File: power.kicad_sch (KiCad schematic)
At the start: 0 parts

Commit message: [#99756] Implement Power section schematic
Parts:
- added C601, C602, C603, C608, C609, C610, C612, C613, C614, C616, C619, C620, C625, C627, C629, C631, C633, C634, C635, C636: C_22u_16V_0603, antmicro-footprints:C_0603_1608Metric_EIA, symbol antmicroCapacitors0603:C_22u_16V_0603
- added C604, C605, C606, C607, C611, C615, C618, C621, C626, C628, C630, C632: C_100n_0402, antmicro-footprints:C_0402_1005Metric, symbol antmicroCapacitors0402:C_100n_0402
- added C617, C622, C623, C624: C_1u_25V_0402, antmicro-footprints:C_0402_1005Metric, symbol antmicroCapacitors0402:C_1u_25V_0402
- added L605: L_2u2_6.3A_Bourns-SRN8040, antmicro-footprints:L_Bourns-SRN8040, symbol antmicroFixedInductors:L_2u2_6.3A_Bourns-SRN8040
- added L606, L607, L608: L_2u2_1.5A_0806, antmicro-footprints:L_0806_2016Metric, symbol antmicroFixedInductors:L_2u2_1.5A_0806
- added R601, R602, R603, R604: R_0R_22.4A_0603, antmicro-footprints:R_0603_1608Metric, symbol antmicroResistors0603:R_0R_22.4A_0603
- added R605: R_255k_0402, antmicro-footprints:R_0402_1005Metric, symbol antmicroResistors0402:R_255k_0402
- added R606, R607, R608, R609, R610: R_100k_0402, antmicro-footprints:R_0402_1005Metric, symbol antmicroResistors0402:R_100k_0402
- added R611, R612, R613: R_0R_0402, antmicro-footprints:R_0402_1005Metric, symbol antmicroResistors0402:R_0R_0402
- added R622: R_73k2_0402, antmicro-footprints:R_0402_1005Metric, symbol antmicroResistors0402:R_73k2_0402
- added R623, R625, R626, R627, R629: R_10k_0402, antmicro-footprints:R_0402_1005Metric, symbol antmicroResistors0402:R_10k_0402
- added R624: R_45k3_0402, antmicro-footprints:R_0402_1005Metric, symbol antmicroResistors0402:R_45k3_0402
- added R628: R_7k5_0402, antmicro-footprints:R_0402_1005Metric, symbol antmicroResistors0402:R_7k5_0402
- added U605, U606, U607, U608: TPS566231P, antmicro-footprints:VQFN-HR-9_2x1.5mm, symbol antmicroDCDCConverters:TPS566231P
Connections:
- new net: C608.2, C609.2, C610.2, C611.2, L606.2, R602.1, R624.2
- new net: C612.2, C613.2, C614.2, C615.2, L607.2, R603.1, R626.2
- new net: C601.2, C602.2, C603.2, C604.2, L605.2, R601.1, R622.2
- new net: C616.2, C619.2, C620.2, C621.2, L608.2, R604.1, R628.2
- new net +12V: C625.2, C626.2, C627.2, C628.2, C629.2, C630.2, C631.2, C632.2, C633.2, C634.2, C635.2, C636.2, R605.2, U605.5 (V_{IN}), U605.6 (V_{IN}), U606.5 (V_{IN}), U606.6 (V_{IN}), U607.5 (V_{IN}), U607.6 (V_{IN}), U608.5 (V_{IN}), U608.6 (V_{IN})
- new net +1V05: R604.2
- new net +1V2: R603.2
- new net +3V3: R602.2
- new net +5V: R601.2
- new net 1V05_BST: C607.1, U608.7 (BST)
- new net 1V05_EN: R612.2, U608.3 (EN)
- new net 1V05_FB: R628.1, R629.2, U608.2 (FB)
- new net 1V05_PG: R608.1, R609.1, R613.1, U606.9 (PG), U608.9 (PG)
- new net 1V05_SW: C607.2, L608.1, U608.8 (SW)
- new net 1V05_VCC: C624.2, R609.2, U608.1 (V_{CC})
- new net 1V2_BST: C606.1, U607.7 (BST)
- new net 1V2_EN: R613.2, U607.3 (EN)
- new net 1V2_FB: R626.1, R627.2, U607.2 (FB)
- new net 1V2_PG: R610.1, U607.9 (PG)
- new net 1V2_SW: C606.2, L607.1, U607.8 (SW)
- new net 1V2_VCC: C623.2, R610.2, U607.1 (V_{CC})
- new net 3V3_BST: C605.1, U606.7 (BST)
- new net 3V3_EN: R611.2, U606.3 (EN)
- new net 3V3_FB: R624.1, R625.2, U606.2 (FB)
- new net 3V3_SW: C605.2, L606.1, U606.8 (SW)
- new net 3V3_VCC: C622.2, R608.2, U606.1 (V_{CC})
- new net 5V_BST: C618.1, U605.7 (BST)
- new net 5V_EN: R605.1, R606.2, U605.3 (EN)
- new net 5V_FB: R622.1, R623.2, U605.2 (FB)
- new net 5V_PG: R607.1, R611.1, R612.1, U605.9 (PG)
- new net 5V_SW: C618.2, L605.1, U605.8 (SW)
- new net 5V_VCC: C617.2, R607.2, U605.1 (V_{CC})
- new net GND: C601.1, C602.1, C603.1, C604.1, C608.1, C609.1, C610.1, C611.1, C612.1, C613.1, C614.1, C615.1, C616.1, C617.1, C619.1, C620.1, C621.1, C622.1, C623.1, C624.1, C625.1, C626.1, C627.1, C628.1, C629.1, C630.1, C631.1, C632.1, C633.1, C634.1, C635.1, C636.1, R606.1, R623.1, R625.1, R627.1, R629.1, U605.4 (PGND), U606.4 (PGND), U607.4 (PGND), U608.4 (PGND)
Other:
- note added: "-->"
- note added: "1V05 DC-DC"
- note added: "1V2"
- note added: "1V2 DC-DC"
- note added: "3V3 & 1V05"
- note added: "3V3 DC-DC"
- note added: "5V"
- note added: "5V DC-DC"
- note added: "UVLO 5V rail is first in the power sequence, so deasserting its enable pin turns off remainng DC-DC converters"
- note added: "V_{OUT} = 0.6 x (1 + R_{H}/R_{L}) [V]"
- note added: "V_{OUT} = 1.05 V"
- note added: "V_{OUT} = 1.2 V"
- note added: "V_{OUT} = 3.318 V"
- note added: "V_{OUT} = 4.992 V"

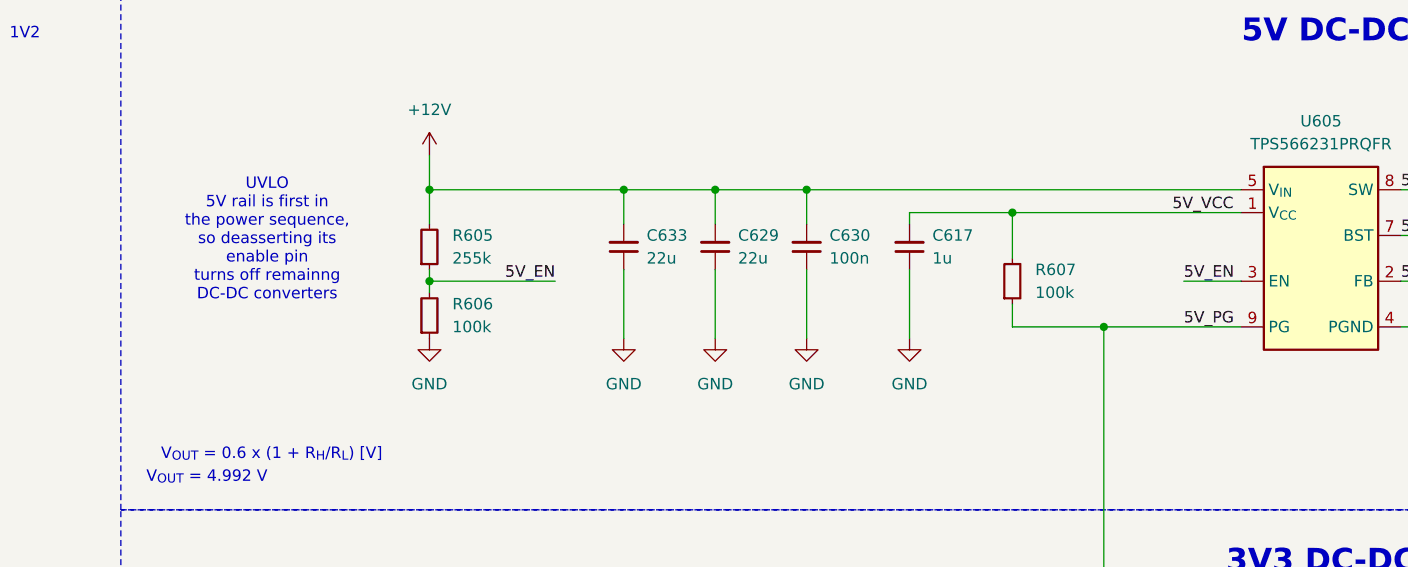
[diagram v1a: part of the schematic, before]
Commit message: [#99756] Change DCDC enable signal
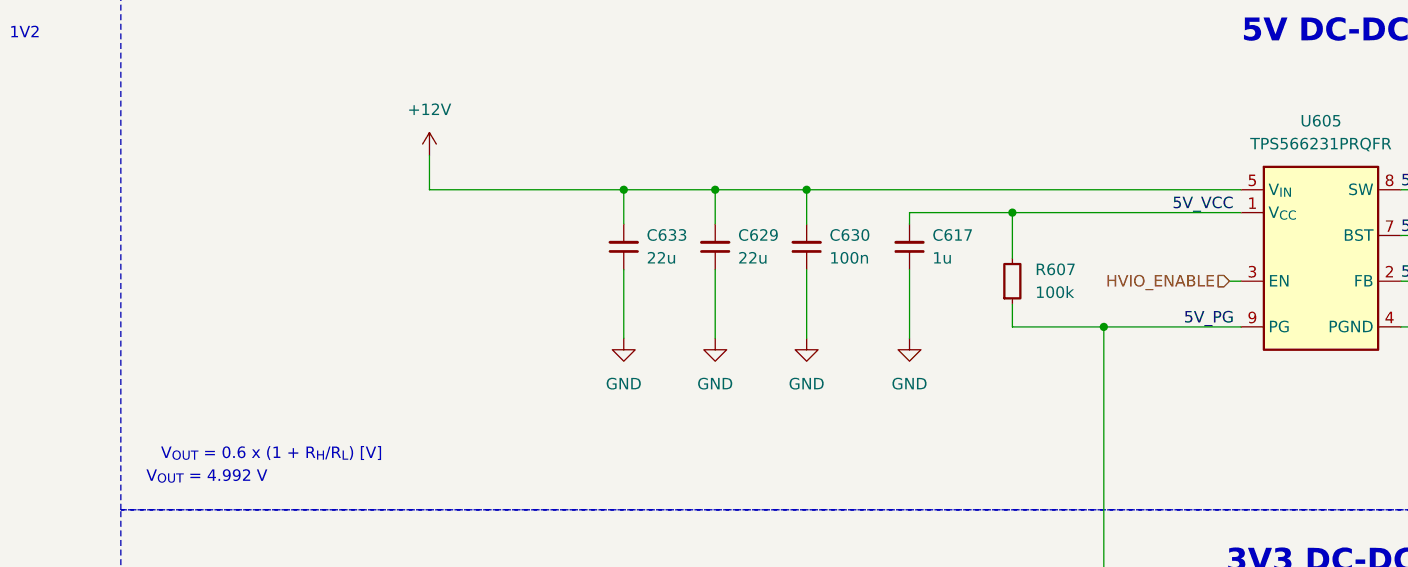
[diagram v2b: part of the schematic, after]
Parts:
- removed R605: R_255k_0402, antmicro-footprints:R_0402_1005Metric, symbol antmicroResistors0402:R_255k_0402
- removed R606: R_100k_0402, antmicro-footprints:R_0402_1005Metric, symbol antmicroResistors0402:R_100k_0402
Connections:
- net 5V_EN renamed HVIO_ENABLE
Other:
- note removed: "UVLO 5V rail is first in the power sequence, so deasserting its enable pin turns off remainng DC-DC converters"

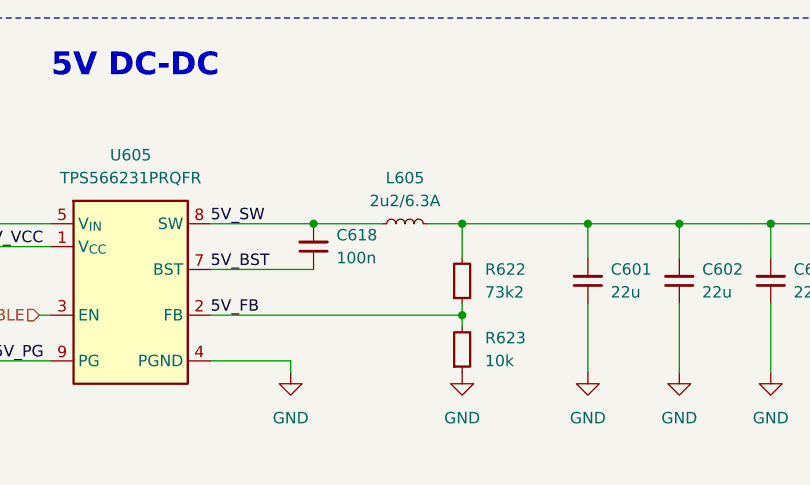
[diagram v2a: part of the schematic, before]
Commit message: [#99756] Change SRN8040 inductor to WE-PMFI-35329222
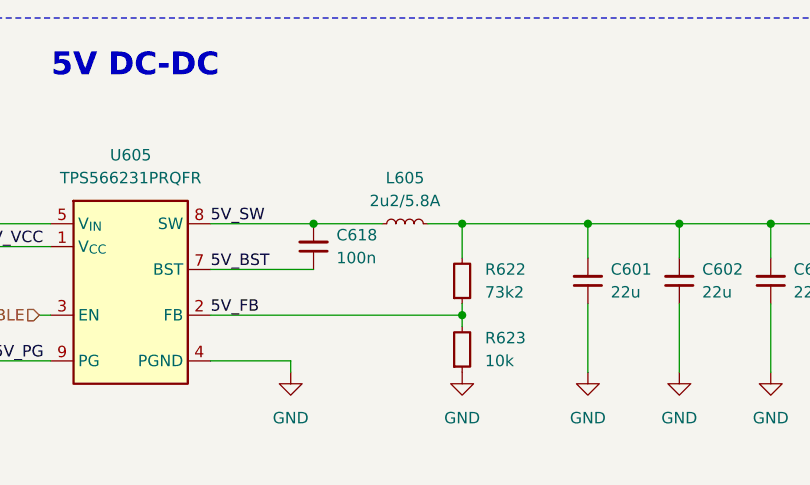
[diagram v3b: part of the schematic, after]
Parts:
- L605: value L_2u2_6.3A_Bourns-SRN8040 -> L_2u2_5.8A_WE-PMFI-35329222; footprint antmicro-footprints:L_Bourns-SRN8040 -> antmicro-footprints:L_WE-PMFI-353220; symbol antmicroFixedInductors:L_2u2_6.3A_Bourns-SRN8040 -> antmicroFixedInductors:L_2u2_5.8A_WE-PMFI-35329222; IMax 6.3 A -> 5.8A; ISat 7.4 A -> 7.8A; MPN SRN8040-2R2Y -> 74479335329222; Manufacturer Bourns -> Würth Elektronik; Size 8.0x8.0 -> 3.5x3.2x2.0; Val 2u2/6.3A -> 2u2/5.8A
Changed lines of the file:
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@@
 	)
 	(symbol
-		(lib_id "antmicroFixedInductors:L_2u2_6.3A_Bourns-SRN8040")
+		(lib_id "antmicroFixedInductors:L_2u2_5.8A_WE-PMFI-35329222")
 		(at 233.68 40.64 0)
 		(unit 1)
@@
 			)
 		)
-		(property "Value" "L_2u2_6.3A_Bourns-SRN8040"
+		(property "Value" "L_2u2_5.8A_WE-PMFI-35329222"
 			(at 247.65 43.18 0)
 			(hide yes)
@@
 			)
 		)
-		(property "Footprint" "antmicro-footprints:L_Bourns-SRN8040"
+		(property "Footprint" "antmicro-footprints:L_WE-PMFI-353220"
 			(at 247.65 48.26 0)
 			(hide yes)
@@
 			)
 		)
-		(property "Datasheet" "https://www.bourns.com/pdfs/SRN8040.pdf"
+		(property "Datasheet" "https://www.we-online.com/components/products/datasheet/74479335329222.pdf"
 			(at 247.65 50.8 0)
 			(hide yes)
@@
 			)
 		)
-		(property "Description" "Power Inductor (SMD), 2.2 µH, 6.3 A, Shielded, 7.4 A, SRN8040 Series"
+		(property "Description" "Power Inductors - SMD WE-PMFI 2.2 uH 5.8 A 40 mOhms AEC-Q200"
 			(at 247.65 71.12 0)
 			(hide yes)
@@
 			)
 		)
-		(property "Val" "2u2/6.3A"
+		(property "Val" "2u2/5.8A"
 			(at 236.22 38.1 0)
 			(show_name no)
@@
 			)
 		)
-		(property "Manufacturer" "Bourns"
+		(property "Manufacturer" "Würth Elektronik"
 			(at 247.65 53.34 0)
 			(hide yes)
@@
 			)
 		)
-		(property "MPN" "SRN8040-2R2Y"
+		(property "MPN" "74479335329222"
 			(at 247.65 55.88 0)
 			(hide yes)
@@
 			)
 		)
-		(property "ISat" "7.4 A"
-			(at 247.65 57.15 0)
+		(property "ISat" "7.8A"
+			(at 247.65 58.42 0)
 			(hide yes)
 			(show_name no)
@@
 					(size 1.27 1.27)
 				)
-				(justify left)
+				(justify left bottom)
 			)
 		)
-		(property "IMax" "6.3 A"
+		(property "IMax" "5.8A"
 			(at 247.65 60.96 0)
 			(hide yes)
@@
 			)
 		)
-		(property "Size" "8.0x8.0"
+		(property "Size" "3.5x3.2x2.0"
 			(at 247.65 63.5 0)
 			(hide yes)
